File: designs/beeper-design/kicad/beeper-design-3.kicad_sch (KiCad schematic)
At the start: 7 parts, among them U12 DRV2605YZFR

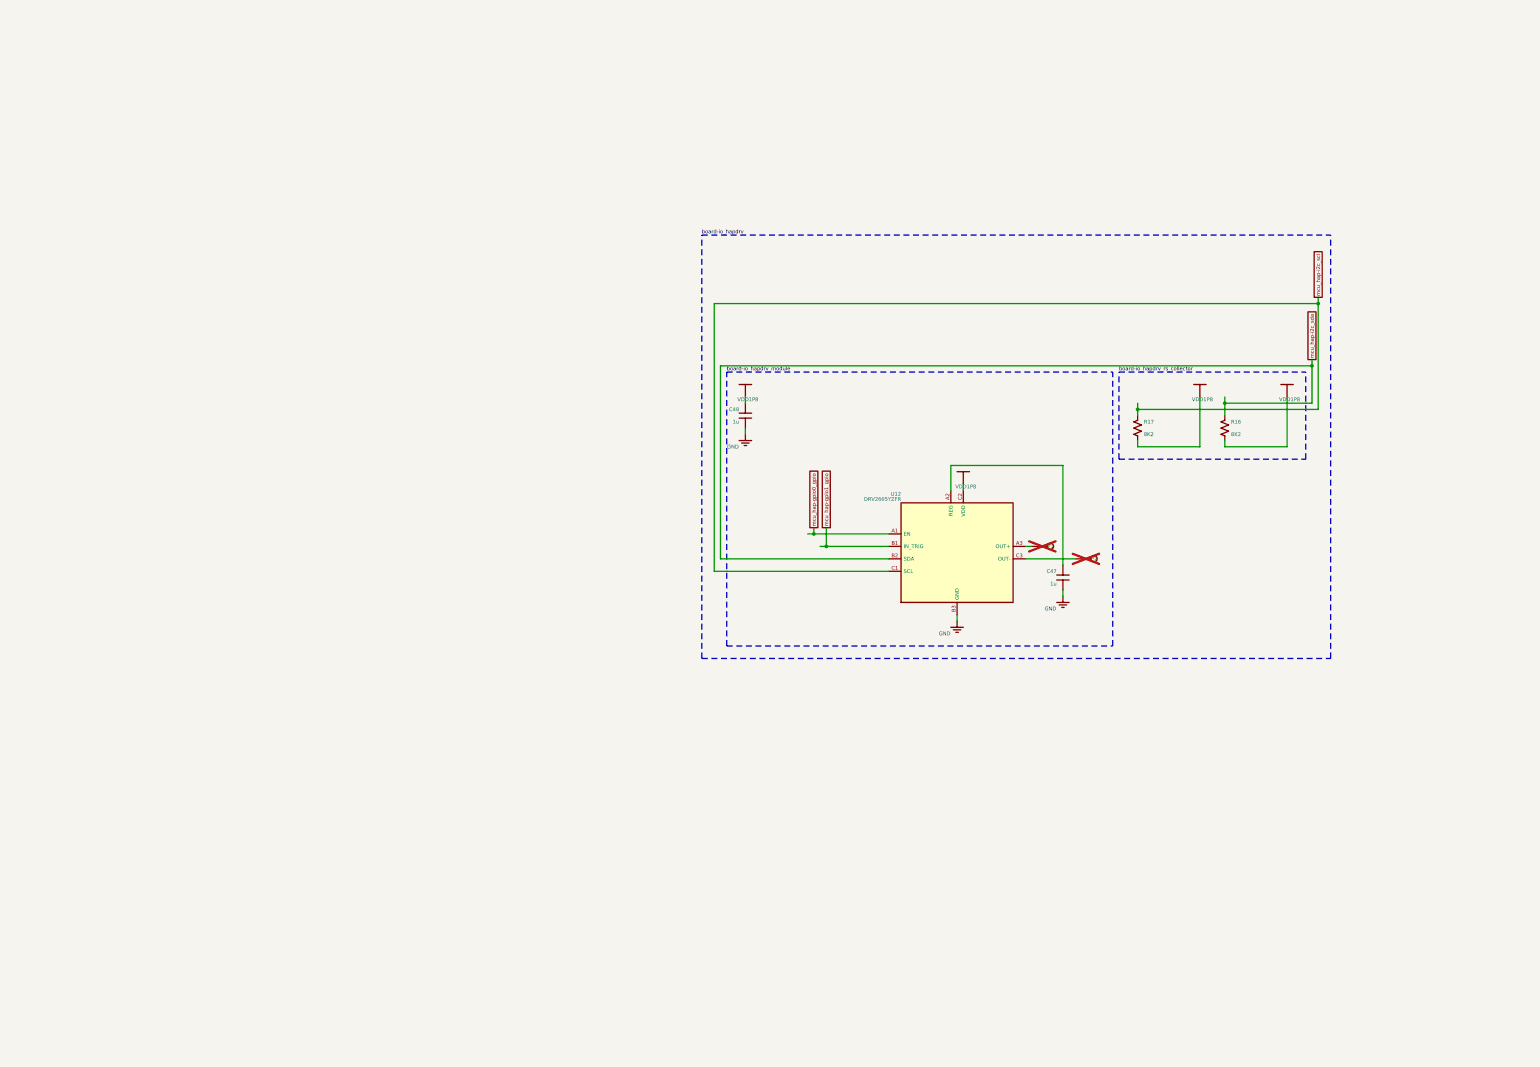
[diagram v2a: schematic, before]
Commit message: fixing drc errors
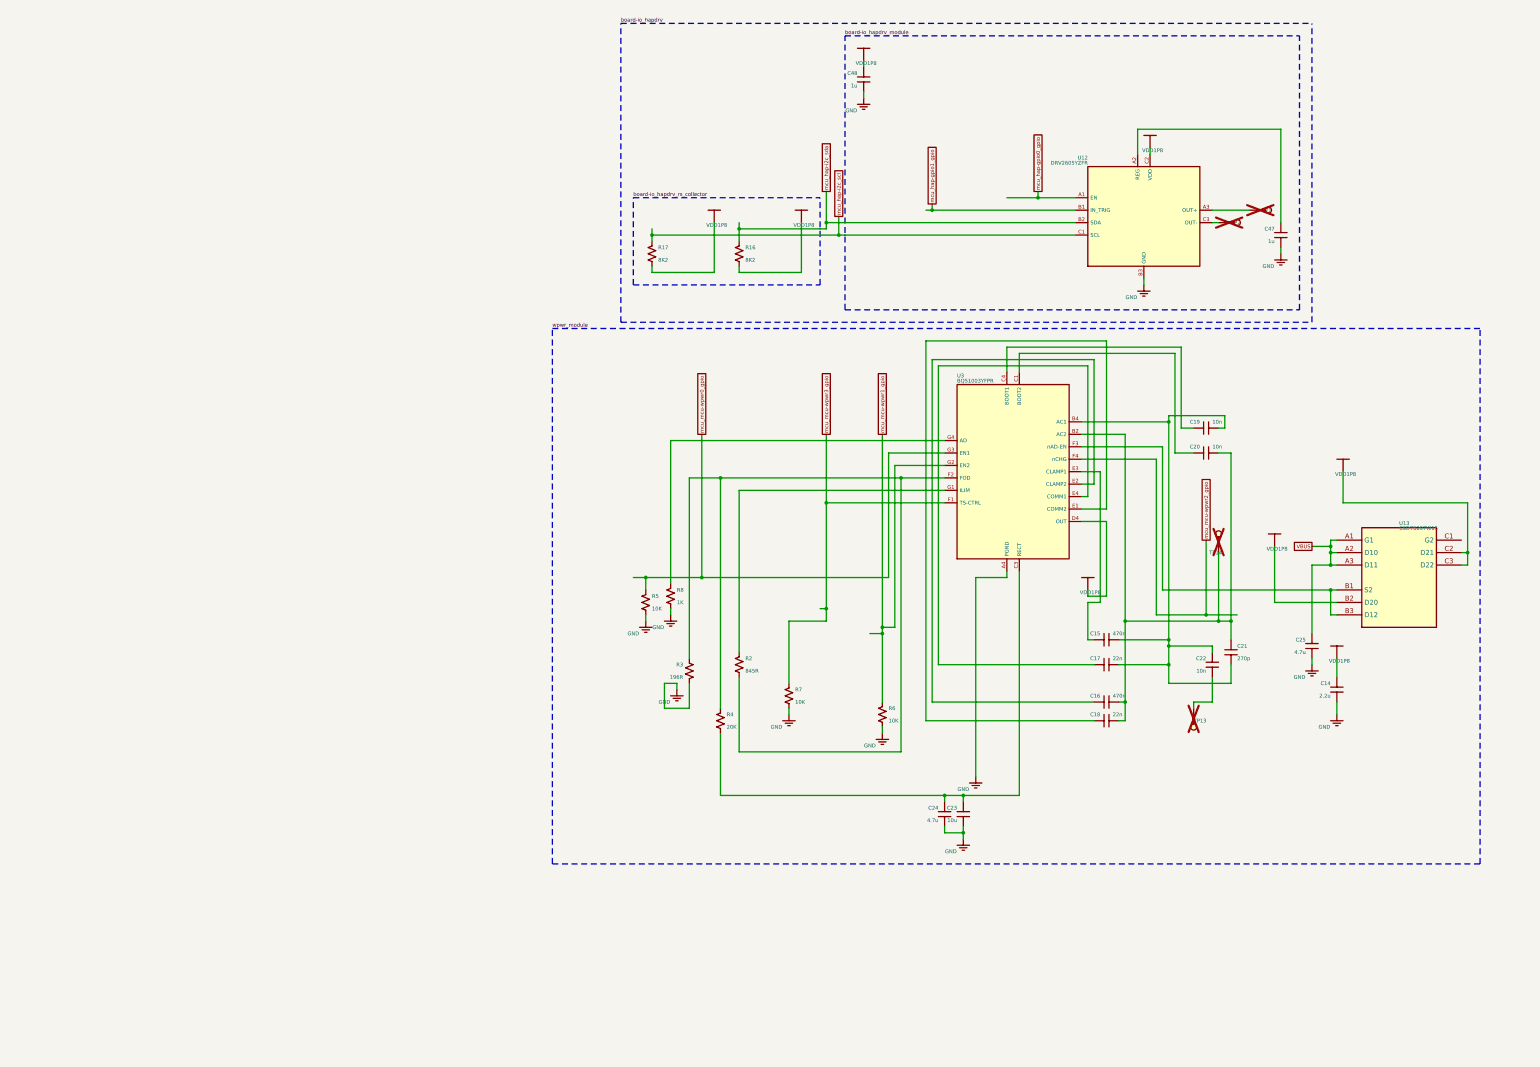
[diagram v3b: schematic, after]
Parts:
- added C14: 2.2u, beeper-design:Pkg0201_25, symbol my_capacitor_7
- added C15: 470n, beeper-design:Pkg0201_21, symbol my_capacitor_5
- added C16: 470n, beeper-design:Pkg0201_31, symbol my_capacitor_10
- added C17: 22n, beeper-design:Pkg0201_45, symbol my_capacitor_18
- added C18: 22n, beeper-design:Pkg0201_9, symbol my_capacitor_2
- added C19: 10n, beeper-design:Pkg0201_18, symbol my_capacitor_4
- added C20: 10n, beeper-design:Pkg0201_30, symbol my_capacitor_9
- added C21: 270p, beeper-design:Pkg0201_43, symbol my_capacitor_16
- added C22: 10n, beeper-design:Pkg0201_7, symbol my_capacitor
- added C23: 10u, beeper-design:Pkg0402_2, symbol C105225_2
- added C24: 4.7u, beeper-design:Pkg0402_6, symbol C23733_1
- added C25: 4.7u, beeper-design:Pkg0402_4, symbol C23733
- added R2: 845R, beeper-design:Pkg0201_36, symbol my_resistor_10
- added R3: 196R, beeper-design:Pkg0201_2, symbol C138167
- added R4: 20K, beeper-design:Pkg0201_12, symbol my_resistor_3
- added R5: 10K, beeper-design:Pkg0201_22, symbol my_resistor_7
- added R6: 10K, beeper-design:Pkg0201_34, symbol my_resistor_9
- added R7: 10K, beeper-design:Pkg0201, symbol my_resistor_12
- added R8: 1K, beeper-design:Pkg0201_11, symbol my_resistor_2
- added TP13, TP14: (no value), beeper-design:SMD_TESTPT, symbol smd_testpoint_cmp
- added U13: CSD75207W15, beeper-design:LP_6, symbol CSD75207W15
- added U3: BQ51003YFPR, beeper-design:LP_7, symbol BQ51003YFPR
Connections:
- net GND: now also C14.1, C23.1, C24.1, C25.1, R3.2, R5.2, R6.2, R7.2, R8.2, U3.A1 (PGND), U3.A2 (PGND), U3.A3 (PGND), U3.A4 (PGND)
- net VDD1P8: now also C14.2, U13.B2 (D20), U13.C2 (D21), U13.C3 (D22), U3.D1 (OUT), U3.D2 (OUT), U3.D3 (OUT), U3.D4 (OUT)
- new net: C16.1, C18.1, C20.1, C21.1, TP14.p, U3.B1 (AC2), U3.B2 (AC2)
- new net: C15.1, C17.1, C19.1, C21.2, C22.2, U3.B3 (AC1), U3.B4 (AC1)
- new net: C17.2, U3.E4 (COMM1)
- new net: R2.2, R3.1, R4.1, U3.F2 (FOD)
- new net: C23.2, C24.2, R4.2, U3.C2 (RECT), U3.C3 (RECT)
- new net: R8.1, U3.G4 (AD)
- new net: C16.2, U3.E2 (CLAMP2)
- new net: C22.1, TP13.p
- new net: C15.2, U3.E3 (CLAMP1)
- new net: U13.B1 (S2), U13.B3 (D12), U3.F3 (nAD-EN)
- new net: R2.1, U3.G1 (ILIM)
- new net: C20.2, U3.C1 (BOOT2)
- new net: C18.2, U3.E1 (COMM2)
- new net: C19.2, U3.C4 (BOOT1)
- new net VBUS: C25.2, U13.A1 (G1), U13.A2 (D10), U13.A3 (D11)
- new net mcu_mcu-wpwr0_gpio: R5.1, U3.G3 (EN1)
- new net mcu_mcu-wpwr1_gpio: R6.1, U3.G2 (EN2)
- new net mcu_mcu-wpwr2_gpio: U3.F4 (nCHG)
- new net mcu_mcu-wpwr3_gpio: R7.1, U3.F1 (TS-CTRL)

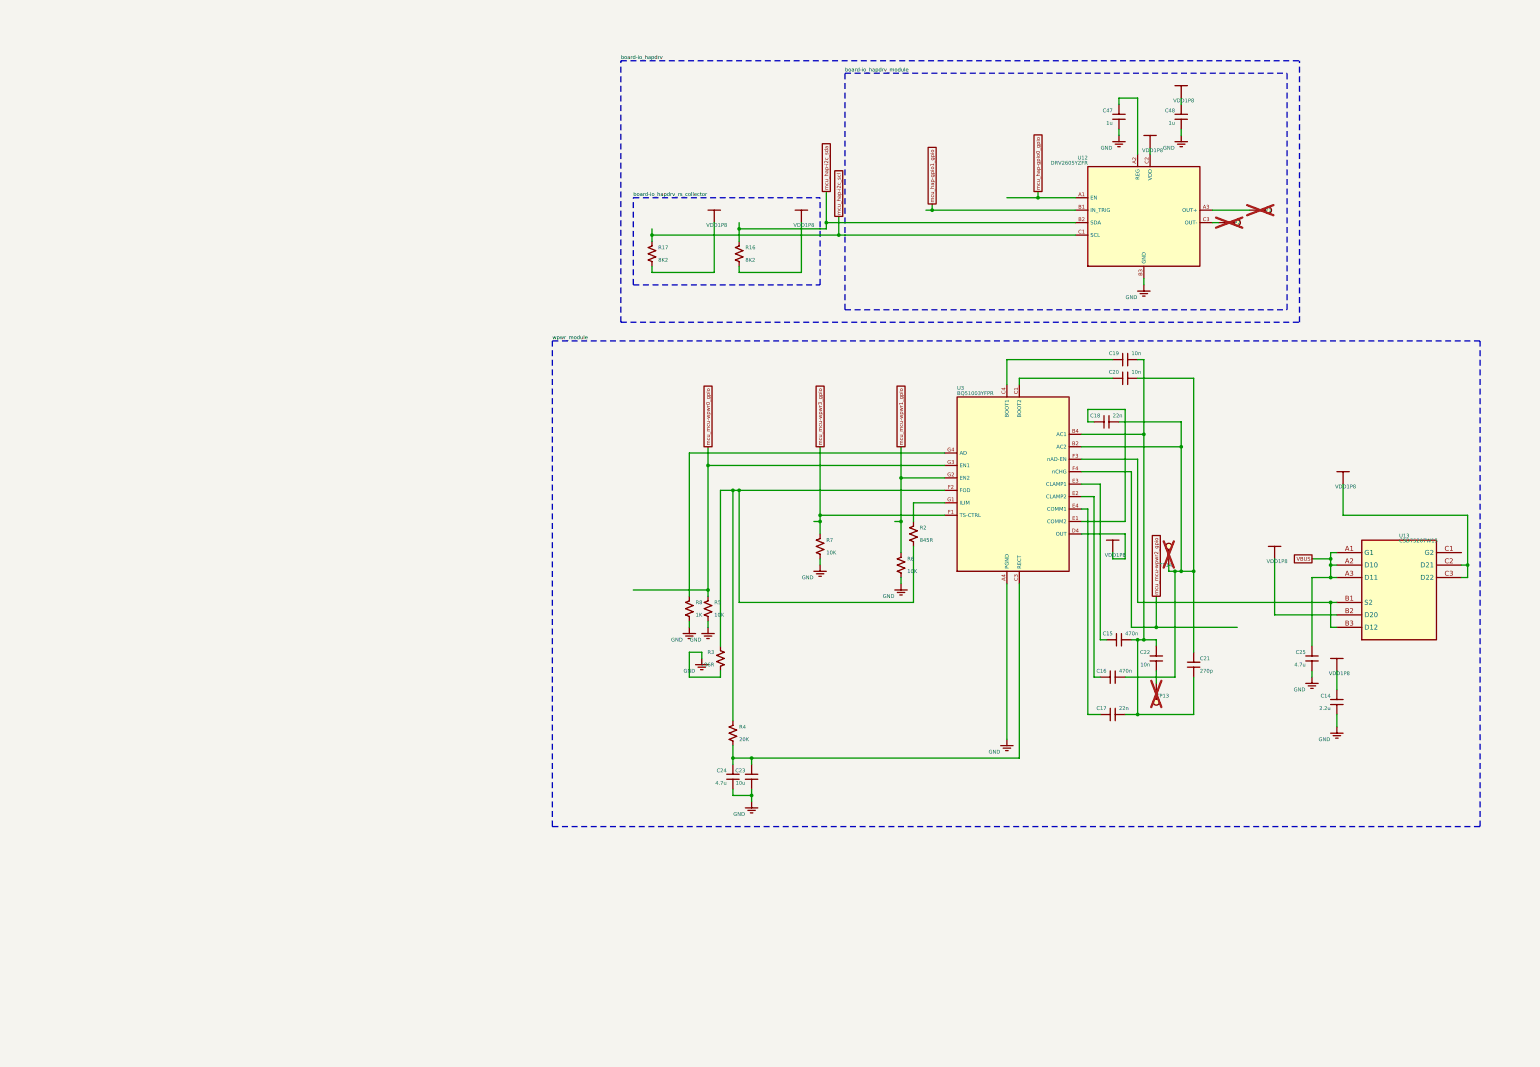
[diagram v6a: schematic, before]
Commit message: made ocdb a submodule
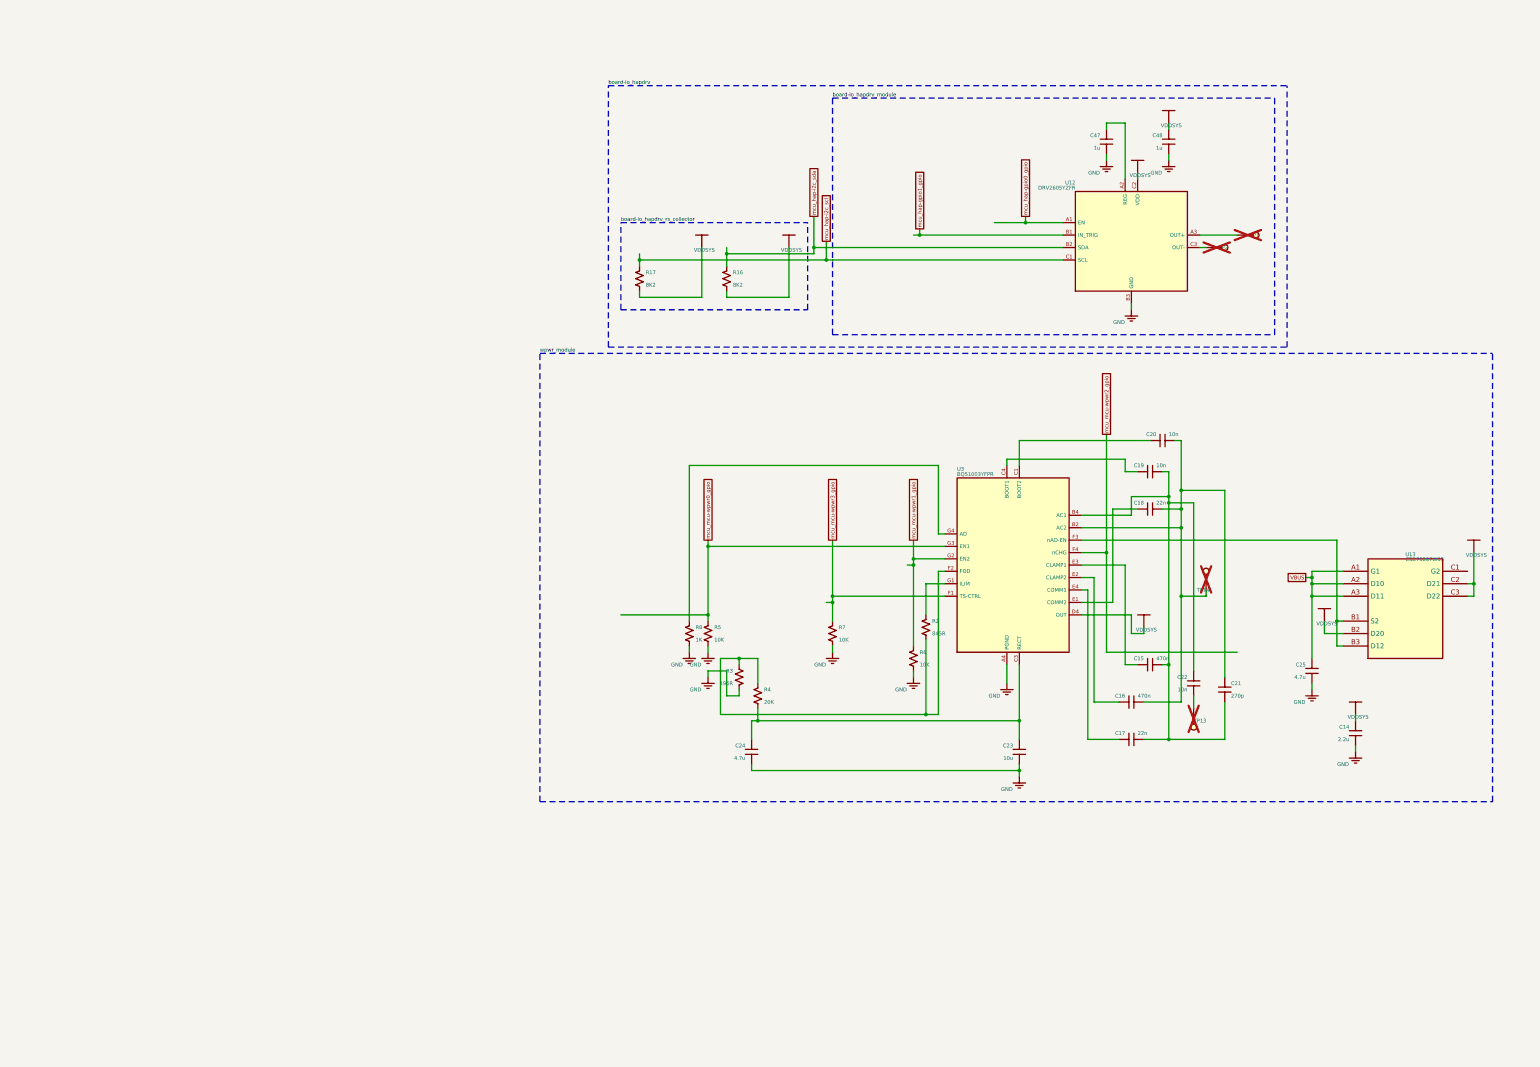
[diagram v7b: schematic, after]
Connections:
- net VDD1P8 renamed VDDSYS

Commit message: kicad exported data
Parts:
- removed C14: 2.2u, beeper-design:Pkg0201_25, symbol my_capacitor_7
- removed C15: 470n, beeper-design:Pkg0201_21, symbol my_capacitor_5
- removed C16: 470n, beeper-design:Pkg0201_31, symbol my_capacitor_10
- removed C17: 22n, beeper-design:Pkg0201_45, symbol my_capacitor_18
- removed C18: 22n, beeper-design:Pkg0201_9, symbol my_capacitor_2
- removed C19: 10n, beeper-design:Pkg0201_18, symbol my_capacitor_4
- removed C20: 10n, beeper-design:Pkg0201_30, symbol my_capacitor_9
- removed C21: 270p, beeper-design:Pkg0201_43, symbol my_capacitor_16
- removed C22: 10n, beeper-design:Pkg0201_7, symbol my_capacitor
- removed C23: 10u, beeper-design:Pkg0402_2, symbol C105225_2
- removed C24: 4.7u, beeper-design:Pkg0402_6, symbol C23733_1
- removed C25: 4.7u, beeper-design:Pkg0402_4, symbol C23733
- removed C47: 1u, beeper-design:Pkg0201_40, symbol C76935_11
- removed C48: 1u, beeper-design:Pkg0201_6, symbol C76935_2
- removed R16, R17: 8K2, beeper-design:Pkg0201_20, symbol my_resistor_6
- removed R2: 845R, beeper-design:Pkg0201_36, symbol my_resistor_10
- removed R3: 196R, beeper-design:Pkg0201_2, symbol C138167
- removed R4: 20K, beeper-design:Pkg0201_12, symbol my_resistor_3
- removed R5: 10K, beeper-design:Pkg0201_22, symbol my_resistor_7
- removed R6: 10K, beeper-design:Pkg0201_34, symbol my_resistor_9
- removed R7: 10K, beeper-design:Pkg0201, symbol my_resistor_12
- removed R8: 1K, beeper-design:Pkg0201_11, symbol my_resistor_2
- added C14: 2.2u, beeper-design:Pkg0201_18, symbol C335106_9
- added C15: 2.2u, beeper-design:Pkg0201_11, symbol C335106_5
- added C16: 2.2u, beeper-design:Pkg0201_27, symbol C335106_17
- added C17: 2.2u, beeper-design:Pkg0201_40, symbol C335106_26
- added C18: 2.2u, beeper-design:Pkg0201_53, symbol C335106_35
- added C19: 2.2u, beeper-design:Pkg0201_10, symbol C335106_4
- added C20: 2.2u, beeper-design:Pkg0201_26, symbol C335106_16
- added C21: 2.2u, beeper-design:Pkg0201_39, symbol C335106_25
- added C22: 2.2u, beeper-design:Pkg0201_52, symbol C335106_34
- added C23: 2.2u, beeper-design:Pkg0201_9, symbol C335106_3
- added C24: 2.2u, beeper-design:Pkg0201_23, symbol C335106_13
- added C25: 2.2u, beeper-design:Pkg0201_16, symbol C335106_7
- added C47: 2.2u, beeper-design:Pkg0201_35, symbol C335106_23
- added C48: 2.2u, beeper-design:Pkg0201_47, symbol C335106_29
- added R16, R17: 8K2, beeper-design:Pkg0201_8, symbol my_resistor_3
- added R2: 845R, beeper-design:Pkg0201_32, symbol my_resistor_7
- added R3: 10K, beeper-design:Pkg0201_30, symbol my_resistor_6
- added R4: 20K, beeper-design:Pkg0201_2, symbol my_resistor
- added R5: 10K, beeper-design:Pkg0201_15, symbol my_resistor_4
- added R6: 196R, beeper-design:Pkg0201_45, symbol C138167
- added R7: 10K, beeper-design:Pkg0201_41, symbol my_resistor_9
- added R8: 1K, beeper-design:Pkg0201_54, symbol my_resistor_12
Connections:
- net GND: now also C14.1, C23.1, C24.1, C25.1, C47.1, C48.1, R3.2, R5.2, R6.2, R7.2, R8.2
- net VBUS: now also C25.2
- net mcu_hap-i2c_scl: now also R17.1
- net mcu_hap-i2c_sda: now also R16.1
- net mcu_mcu-wpwr0_gpio: now also R5.1
- net mcu_mcu-wpwr1_gpio: now also R3.1
- net mcu_mcu-wpwr3_gpio: now also R7.1
- net at TP14.p, U3.B1 (AC2), U3.B2 (AC2): now also C16.1, C18.1, C20.1, C21.1
- net at U3.E2 (CLAMP2): now also C16.2
- net at U12.A2 (REG): now also C47.2
- net at U3.G4 (AD): now also R8.1
- net at U3.C2 (RECT), U3.C3 (RECT): now also C23.2, C24.2, R4.2
- net at TP13.p: now also C22.1
- net at U3.B3 (AC1), U3.B4 (AC1): now also C15.1, C17.1, C19.1, C21.2, C22.2
- net at U3.F2 (FOD): now also R2.2, R4.1, R6.1
- net at U3.G1 (ILIM): now also R2.1
- net at U3.C4 (BOOT1): now also C19.2
- net at U3.E3 (CLAMP1): now also C15.2
- net at U3.C1 (BOOT2): now also C20.2
- net at U3.E4 (COMM1): now also C17.2
- net at U3.E1 (COMM2): now also C18.2
- net VDDSYS renamed VDD1P8
- net VDD1P8: now also C14.2, C48.2, R16.2, R17.2
